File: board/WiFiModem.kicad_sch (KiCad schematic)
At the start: 46 parts, among them J1 DB9_Female, J2 DB25_Female, J3 Barrel_Jack_Switch, J4 PRG, SW1 SW_Push, SW2 SW_Push, U1 ESP-12E, U2 LM7805_TO220, U3 MAX232, U4 LT1117-3.3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

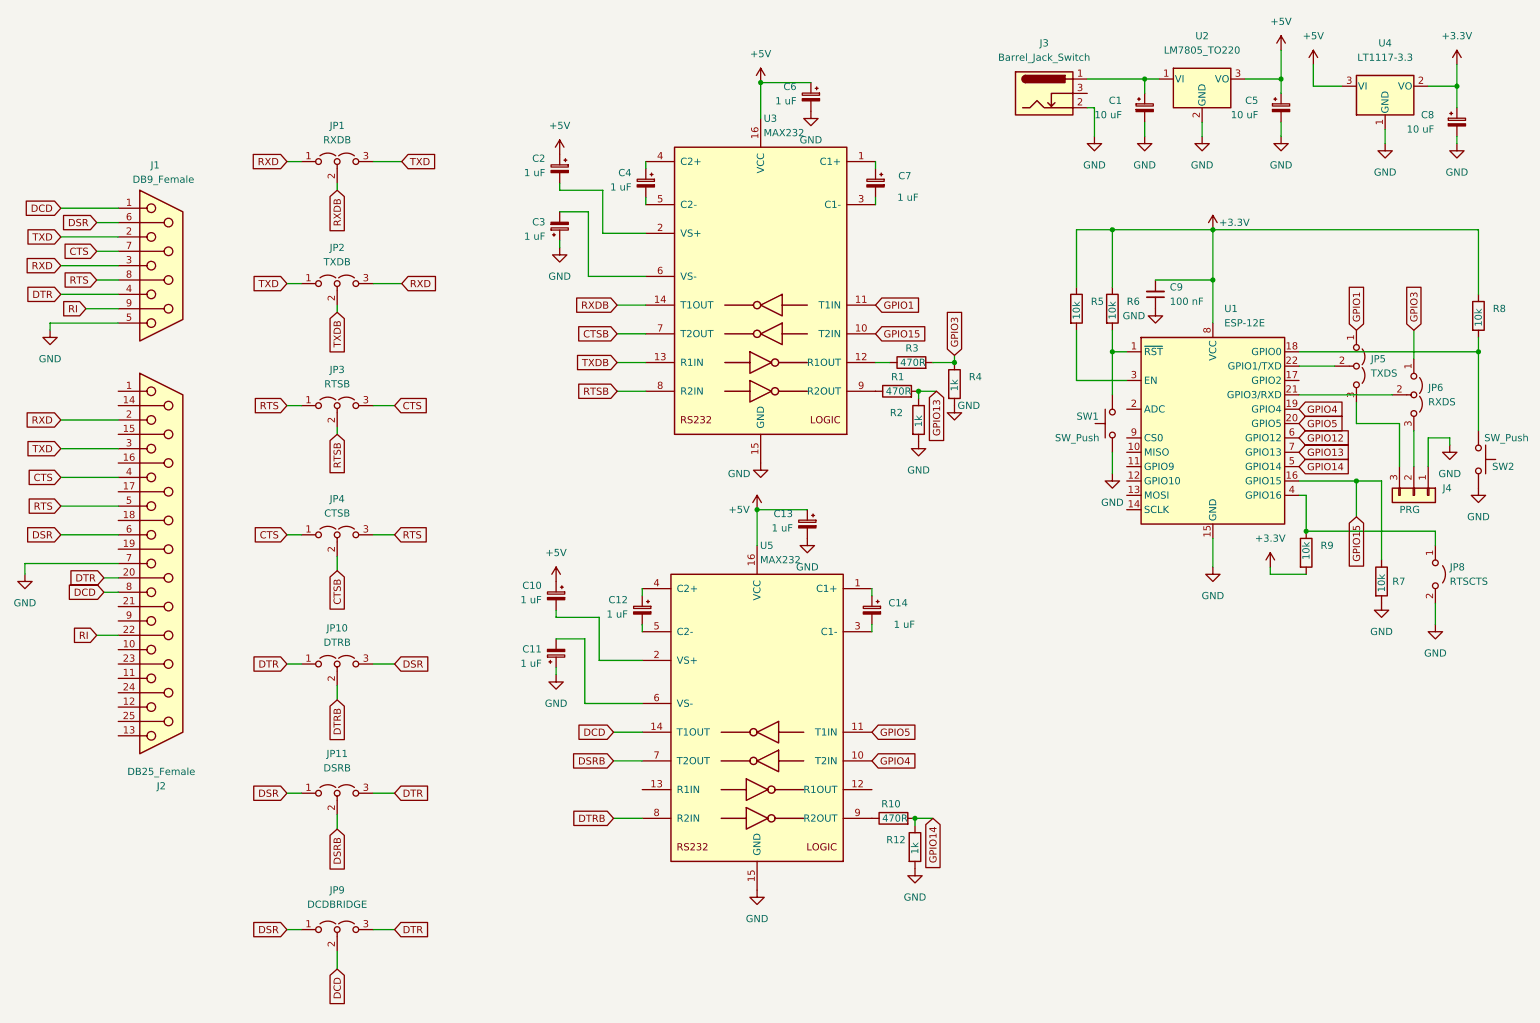
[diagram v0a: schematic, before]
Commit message: Fix KiCAD 7.x DRC warnings.
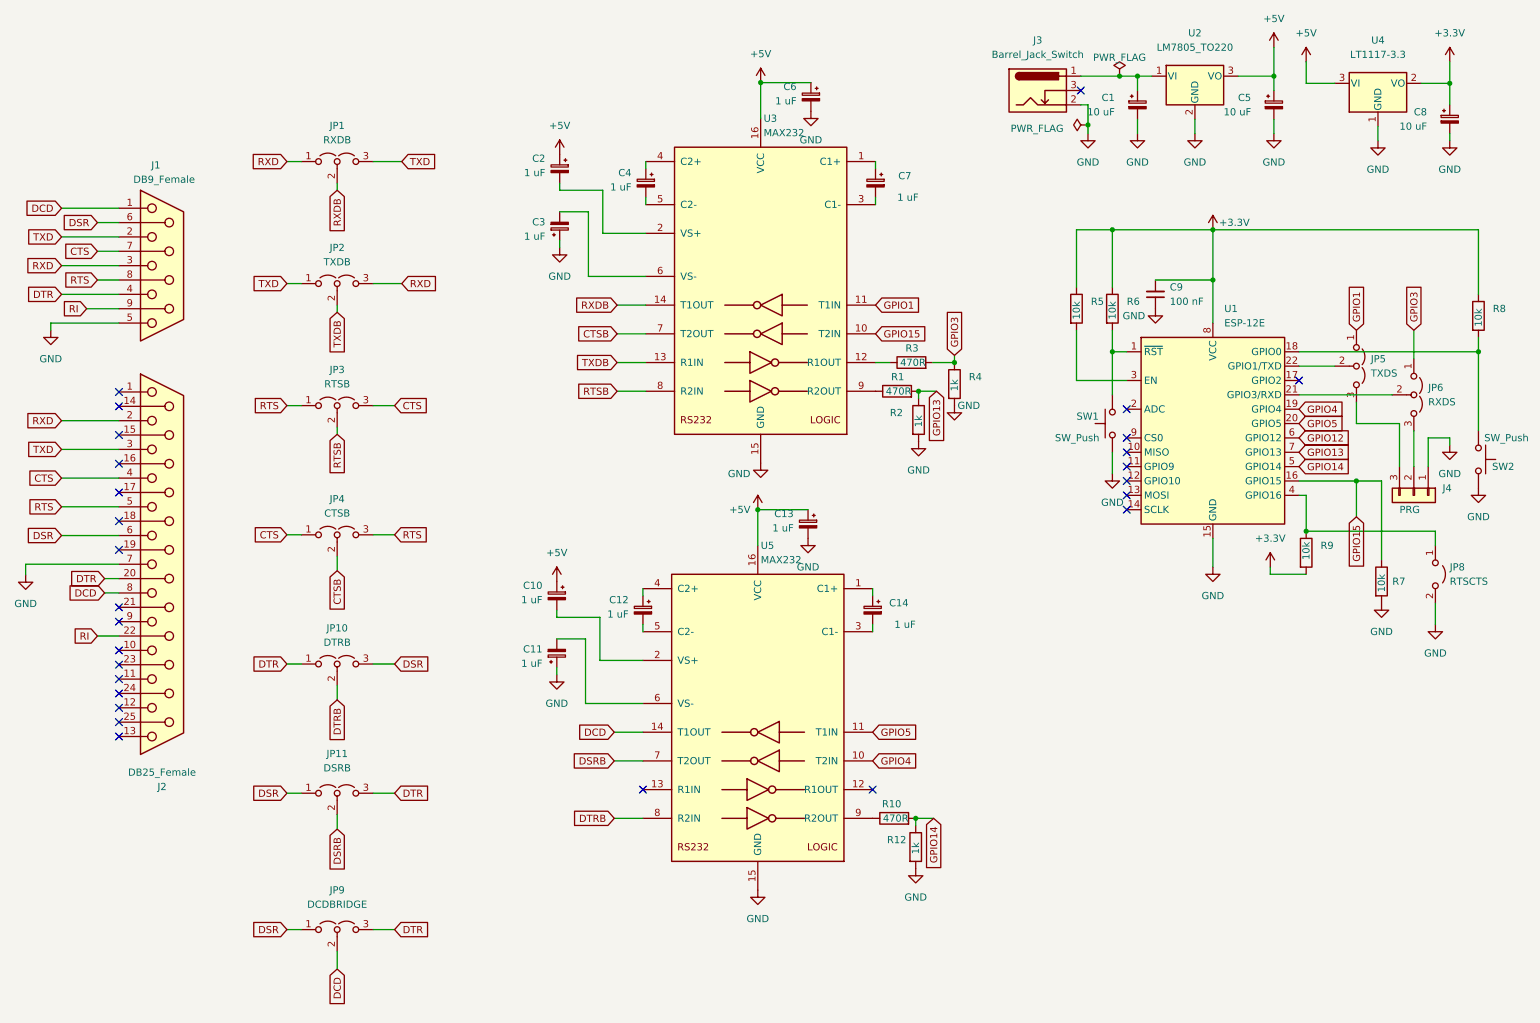
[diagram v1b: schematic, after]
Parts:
- J1: symbol Connector:DB9_Female -> Connector:DE9_Receptacle
- J2: symbol Connector:DB25_Female -> Connector:DB25_Receptacle
- U2: footprint Package_TO_SOT_THT:TO-220-3_Horizontal_TabDown -> Package_TO_SOT_THT:TO-220-3_Vertical
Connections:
- net +3V3 renamed +3.3V
- no-connect marks 0 -> 27
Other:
- moved on the sheet: C1, C5, C8, J3, U2, U4
